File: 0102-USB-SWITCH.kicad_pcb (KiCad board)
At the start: 2 copper layers, 42.1 x 24.6 mm, 11 parts, among them J1 UPSTREAM, J2 DOWNSTREAM, SW1 EN

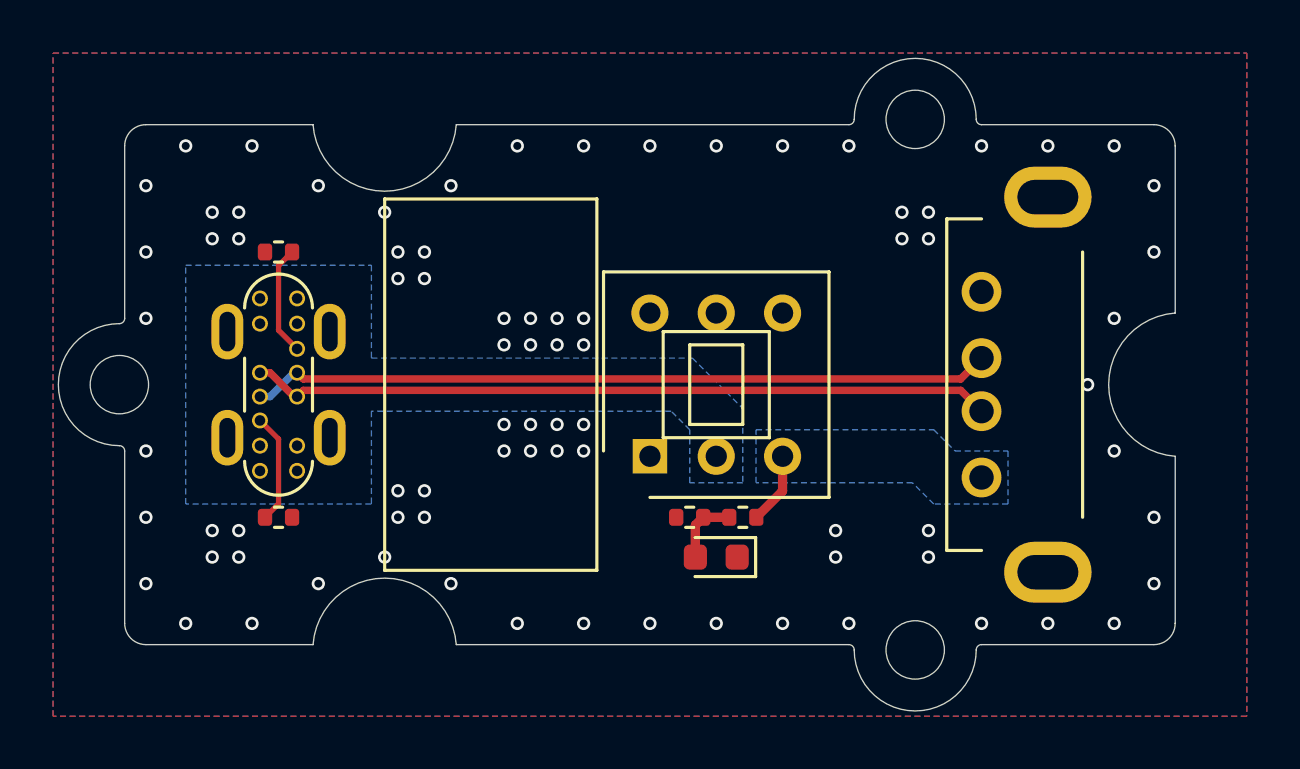
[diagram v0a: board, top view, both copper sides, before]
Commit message: Rework PCB for kibuzzard silk and laying USB-A slot
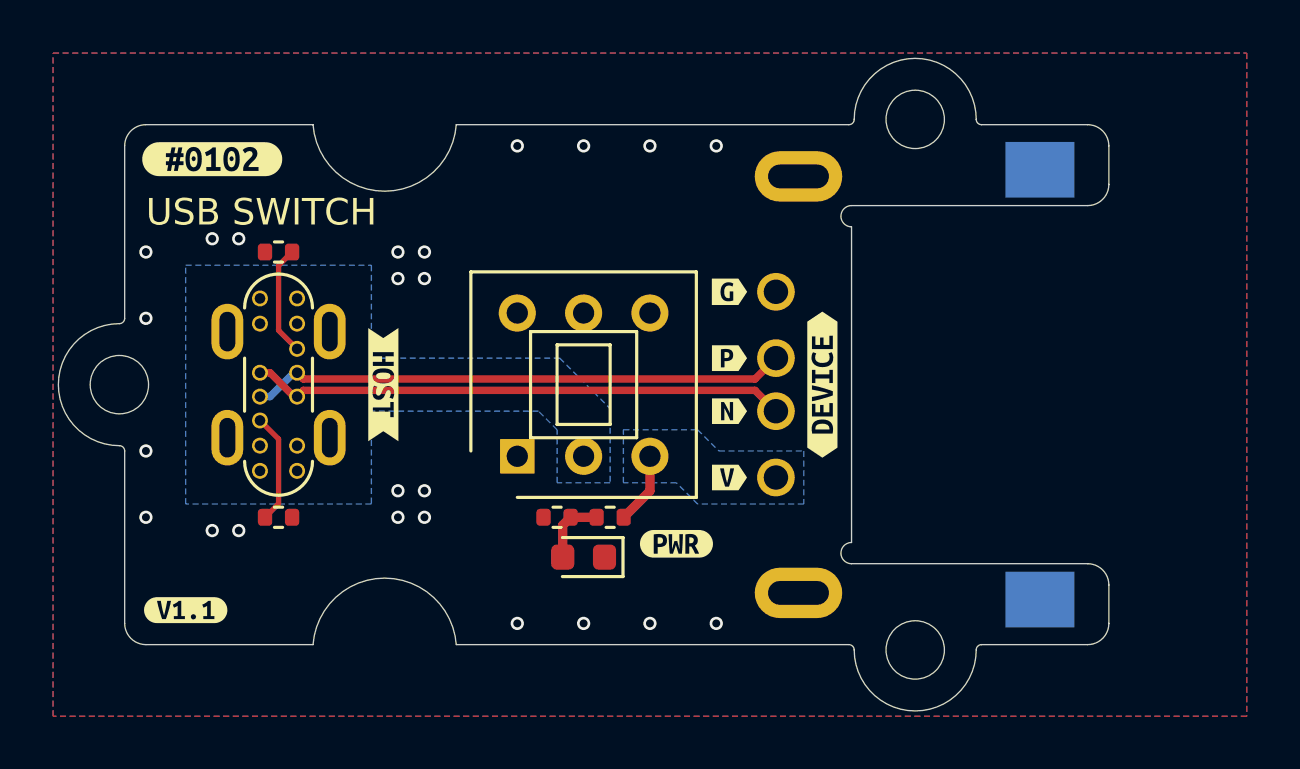
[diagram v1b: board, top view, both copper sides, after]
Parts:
- added kibuzzard-631FFD2B: G***, kibuzzard-631FFD2B, F.Cu at (103.5, 101.5)
- added kibuzzard-631FFD46: G***, kibuzzard-631FFD46, F.Cu at (102.5, 118.5)
- added kibuzzard-631FFEA9: G***, kibuzzard-631FFEA9, F.Cu at (121.0, 116.0)
- added kibuzzard-631FFF00: G***, kibuzzard-631FFF00, F.Cu at (110.0, 110.0)
- added kibuzzard-631FFF07: G***, kibuzzard-631FFF07, F.Cu at (126.5, 110.0)
- added kibuzzard-63200097: G***, kibuzzard-63200097, F.Cu at (123.0, 109.0)
- added kibuzzard-6320009C: G***, kibuzzard-6320009C, F.Cu at (123.0, 106.5)
- added kibuzzard-632000A0: G***, kibuzzard-632000A0, F.Cu at (123.0, 111.0)
- added kibuzzard-632000A4: G***, kibuzzard-632000A4, F.Cu at (123.0, 113.5)
- J2: footprint JLC-SMT:CKMTW_USBAS04P -> JLC-SMT:MOLEX_48258-0001; moved to B.Cu
- moved J2 6.90 mm to (125.6, 110.0), turned to -90 degrees
- moved D1 5.00 mm to (117.5, 116.5)
- moved R1 5.00 mm to (118.5, 115.0)
- moved R2 5.00 mm to (116.5, 115.0)
- moved SW1 5.00 mm to (117.5, 110.0)
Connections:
- J1 pad S1: Net-(J1-PadS1) -> unconnected-(J1-PadS1)
- J2 pad 5: Net-(J2-Pad5) -> unconnected-(J2-Pad5)
- SW1 pad 1: (no net) -> unconnected-(SW1-Pad1)
- SW1 pad 4: (no net) -> unconnected-(SW1-Pad4)
- SW1 pad 5: (no net) -> unconnected-(SW1-Pad5)
- SW1 pad 6: (no net) -> unconnected-(SW1-Pad6)
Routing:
- net /D-: track 28.0 -> 20.2 mm
- net /D+: track 28.0 -> 20.2 mm
- net GND: vias 81 -> 24
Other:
- board size 42.1 x 24.6 mm -> 39.6 x 24.6 mm
- board text added: "USB SWITCH"
- board text removed: "#0102 USB-C V1.1"

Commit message: Rework with new design
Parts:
- removed H1, H2, H3: MountingHole, MountingHole:MountingHole_2.2mm_M2
- removed kibuzzard-631FFD46: G***, kibuzzard-631FFD46
- removed kibuzzard-631FFF00: G***, kibuzzard-631FFF00
- removed kibuzzard-631FFF07: G***, kibuzzard-631FFF07
- removed kibuzzard-63200097: G***, kibuzzard-63200097
- removed kibuzzard-6320009C: G***, kibuzzard-6320009C
- removed kibuzzard-632000A0: G***, kibuzzard-632000A0
- removed kibuzzard-632000A4: G***, kibuzzard-632000A4
- added kibuzzard-632D82D3: G***, kibuzzard-632D82D3, B.Cu at (123.0, 106.5)
- added kibuzzard-632D82DD: G***, kibuzzard-632D82DD, B.Cu at (123.0, 109.0)
- added kibuzzard-632D82E6: G***, kibuzzard-632D82E6, B.Cu at (123.0, 111.0)
- added kibuzzard-632D82EF: G***, kibuzzard-632D82EF, B.Cu at (123.0, 113.5)
- added kibuzzard-632D83AE: G***, kibuzzard-632D83AE, F.Cu at (102.5, 118.5)
- J1: footprint JLC-SMT:KINGHELM_KH-TYPE-C-L10-14P -> JLC-SMT:HRO_TYPE-C-31-M-12
- J2: moved to F.Cu
- moved R4 7.98 mm to (110.2, 111.8), turned to 180 degrees
- moved R3 7.56 mm to (110.2, 108.8)
- moved J1 2.01 mm to (104.0, 110.0), turned to -90 degrees
- moved D1 1.00 mm to (116.5, 116.5)
- moved R1 1.00 mm to (117.5, 115.0)
- moved R2 1.00 mm to (115.5, 115.0)
- moved SW1 1.00 mm to (116.5, 110.0)
- moved kibuzzard-631FFEA9 1.00 mm to (120.0, 116.0)
- turned J2 to 90 degrees
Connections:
- J1 pad S1: unconnected-(J1-PadS1) -> GND
- J2 pad 5: unconnected-(J2-Pad5) -> GND
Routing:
- net /VIN: track 0.00 -> 18.5 mm, vias 0 -> 2
- net /VOUT: track 2.71 -> 12.0 mm
- net Net-(J1-PadB5): track 4.15 -> 1.70 mm
- net Net-(J1-PadA5): track 4.15 -> 1.70 mm
- net /D-: track 20.2 -> 19.3 mm
- net GND: vias 24 -> 22
- removed copper zone on B.Cu, net /VIN
- removed copper zone on B.Cu, net /VOUT
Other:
- board size 39.6 x 24.6 mm -> 37.1 x 19.6 mm

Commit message: Output MF docs V1.2
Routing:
- net GND: vias 22 -> 35
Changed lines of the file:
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@@
     (at 103.99 110 -90)
     (property "Manufacturer" "HRO")
-    (property "PartNumber" "")
+    (property "PartNumber" "C165948")
     (property "Sheetfile" "0102-USB-SWITCH.kicad_sch")
     (property "Sheetname" "")
@@
   (gr_circle (center 130 120) (end 132 120) (layer "F.CrtYd") (width 0.05) (fill none))
   (gr_circle (center 130 100) (end 132 100) (layer "F.CrtYd") (width 0.05) (fill none))
-  (gr_text "USB SWITCH" (at 101 103.5) (layer "F.SilkS")
+  (gr_text "USB SWITCH" (at 101 103) (layer "F.SilkS")
     (effects (font (size 1 1) (thickness 0.15)) (justify left))
   )
@@
   (segment (start 110.410944 109.785) (end 123.965 109.785) (width 0.28) (layer "F.Cu") (net 2))
   (segment (start 109.122501 110.25) (end 109.157501 110.285) (width 0.28) (layer "F.Cu") (net 2))
-  (via (at 110.9 115.8) (size 0.5) (drill 0.3) (layers "F.Cu" "B.Cu") (net 3))
-  (via (at 110.9 116.8) (size 0.5) (drill 0.3) (layers "F.Cu" "B.Cu") (net 3))
-  (via (at 110.5 106) (size 0.5) (drill 0.3) (layers "F.Cu" "B.Cu") (net 3))
-  (via (at 110.5 105) (size 0.5) (drill 0.3) (layers "F.Cu" "B.Cu") (net 3))
-  (via (at 104.5 115.5) (size 0.5) (drill 0.3) (layers "F.Cu" "B.Cu") (net 3))
-  (via (at 104.5 104.5) (size 0.5) (drill 0.3) (layers "F.Cu" "B.Cu") (net 3))
-  (via (at 111.5 105) (size 0.5) (drill 0.3) (layers "F.Cu" "B.Cu") (net 3))
-  (via (at 111.9 115.8) (size 0.5) (drill 0.3) (layers "F.Cu" "B.Cu") (net 3))
+  (via (at 110 114.5) (size 0.5) (drill 0.3) (layers "F.Cu" "B.Cu") (net 3))
+  (via (at 110 115.5) (size 0.5) (drill 0.3) (layers "F.Cu" "B.Cu") (net 3))
+  (via (at 110 105.5) (size 0.5) (drill 0.3) (layers "F.Cu" "B.Cu") (net 3))
+  (via (at 110 104.5) (size 0.5) (drill 0.3) (layers "F.Cu" "B.Cu") (net 3))
+  (via (at 101 110) (size 0.5) (drill 0.3) (layers "F.Cu" "B.Cu") (free) (net 3))
+  (via (at 122 104) (size 0.5) (drill 0.3) (layers "F.Cu" "B.Cu") (free) (net 3))
+  (via (at 111 104.5) (size 0.5) (drill 0.3) (layers "F.Cu" "B.Cu") (net 3))
+  (via (at 111 114.5) (size 0.5) (drill 0.3) (layers "F.Cu" "B.Cu") (net 3))
   (via (at 117.5 119) (size 0.5) (drill 0.3) (layers "F.Cu" "B.Cu") (net 3))
+  (via (at 112.5 101) (size 0.5) (drill 0.3) (layers "F.Cu" "B.Cu") (free) (net 3))
+  (via (at 114 115) (size 0.5) (drill 0.3) (layers "F.Cu" "B.Cu") (free) (net 3))
   (via (at 115 119) (size 0.5) (drill 0.3) (layers "F.Cu" "B.Cu") (net 3))
+  (via (at 123 116) (size 0.5) (drill 0.3) (layers "F.Cu" "B.Cu") (free) (net 3))
+  (via (at 107.5 119) (size 0.5) (drill 0.3) (layers "F.Cu" "B.Cu") (free) (net 3))
+  (via (at 122 116) (size 0.5) (drill 0.3) (layers "F.Cu" "B.Cu") (free) (net 3))
+  (via (at 118.5 116.5) (size 0.5) (drill 0.3) (layers "F.Cu" "B.Cu") (free) (net 3))
+  (via (at 101 112.5) (size 0.5) (drill 0.3) (layers "F.Cu" "B.Cu") (free) (net 3))
   (via (at 115 101) (size 0.5) (drill 0.3) (layers "F.Cu" "B.Cu") (net 3))
   (via (at 120 101) (size 0.5) (drill 0.3) (layers "F.Cu" "B.Cu") (net 3))
-  (via (at 111.5 106) (size 0.5) (drill 0.3) (layers "F.Cu" "B.Cu") (net 3))
+  (via (at 122 105) (size 0.5) (drill 0.3) (layers "F.Cu" "B.Cu") (free) (net 3))
+  (via (at 101 107.5) (size 0.5) (drill 0.3) (layers "F.Cu" "B.Cu") (free) (net 3))
+  (via (at 107.5 101) (size 0.5) (drill 0.3) (layers "F.Cu" "B.Cu") (free) (net 3))
+  (via (at 111 105.5) (size 0.5) (drill 0.3) (layers "F.Cu" "B.Cu") (net 3))
   (via (at 101 105) (size 0.5) (drill 0.3) (layers "F.Cu" "B.Cu") (net 3))
   (via (at 120 119) (size 0.5) (drill 0.3) (layers "F.Cu" "B.Cu") (net 3))
@@
   (via (at 117.5 101) (size 0.5) (drill 0.3) (layers "F.Cu" "B.Cu") (net 3))
   (via (at 122.5 119) (size 0.5) (drill 0.3) (layers "F.Cu" "B.Cu") (free) (net 3))
-  (via (at 111.9 116.8) (size 0.5) (drill 0.3) (layers "F.Cu" "B.Cu") (net 3))
-  (via (at 103.5 115.5) (size 0.5) (drill 0.3) (layers "F.Cu" "B.Cu") (net 3))
+  (via (at 112.5 119) (size 0.5) (drill 0.3) (layers "F.Cu" "B.Cu") (free) (net 3))
+  (via (at 111 115.5) (size 0.5) (drill 0.3) (layers "F.Cu" "B.Cu") (net 3))
+  (via (at 123 115) (size 0.5) (drill 0.3) (layers "F.Cu" "B.Cu") (free) (net 3))
+  (via (at 122 115) (size 0.5) (drill 0.3) (layers "F.Cu" "B.Cu") (free) (net 3))
   (via (at 101 115) (size 0.5) (drill 0.3) (layers "F.Cu" "B.Cu") (net 3))
-  (via (at 103.5 104.5) (size 0.5) (drill 0.3) (layers "F.Cu" "B.Cu") (net 3))
+  (via (at 123 105) (size 0.5) (drill 0.3) (layers "F.Cu" "B.Cu") (free) (net 3))
+  (via (at 123 104) (size 0.5) (drill 0.3) (layers "F.Cu" "B.Cu") (free) (net 3))
   (segment (start 109.15 112.4) (end 110 113.25) (width 0.5) (layer "F.Cu") (net 4))
   (segment (start 108.035 112.4) (end 109.15 112.4) (width 0.5) (layer "F.Cu") (net 4))
